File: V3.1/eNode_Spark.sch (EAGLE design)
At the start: 70 parts, among them U1 WM-N-BM-09, U10 OPA344, U2 MCP73831T-2ACI/OT, U3 R8008-33, U5 HTU21DSMD, U6 TMP006, U7 BMP180, U8 USD-SOCKETSMD, U9 MIC9.7MM, X1 USB-MICROB

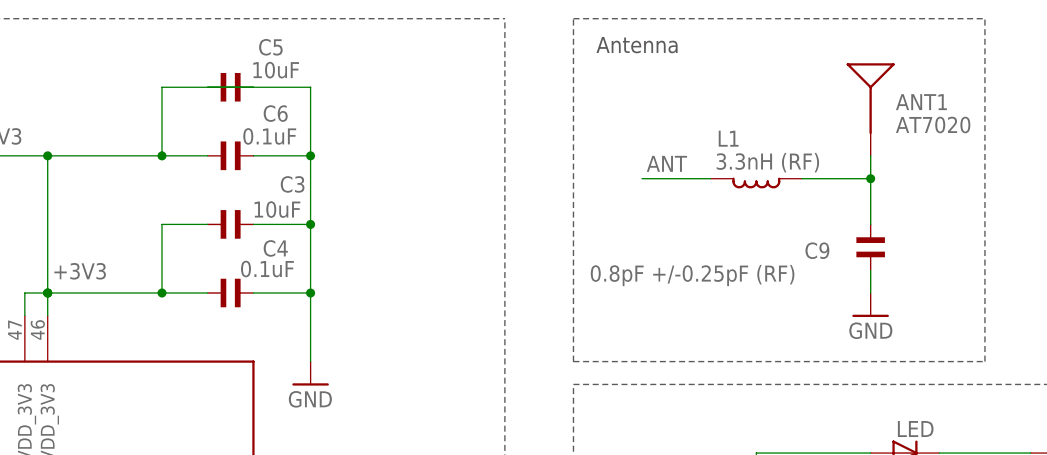
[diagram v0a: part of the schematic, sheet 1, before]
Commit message: Fully Routed
Fully Routed, DRC checked, Gerbers generated
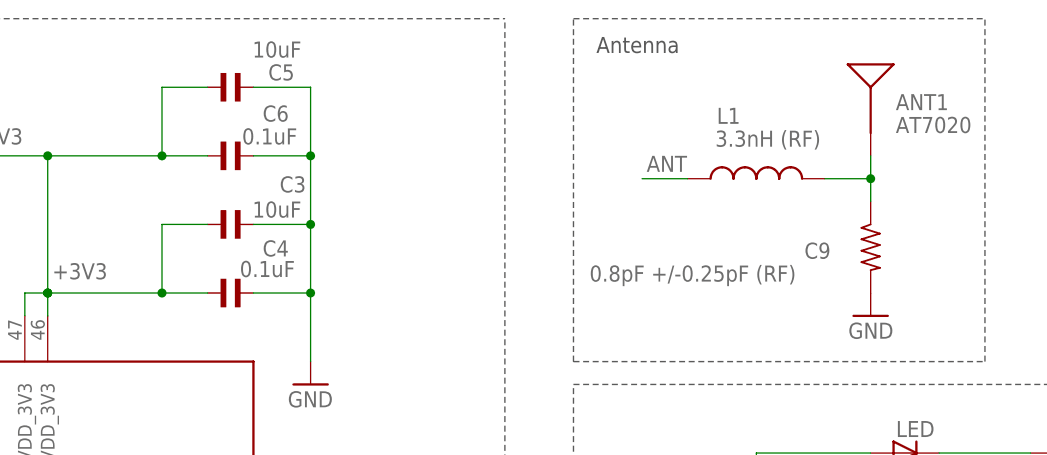
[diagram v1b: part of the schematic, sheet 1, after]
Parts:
- C9: device rc-master-smd:C_0402 -> Spark:R-US_
- L1: device rc-master-smd:L_0402 -> Spark:INDUCTOR
- R6, R7: device rc-master-smd:R_0603 -> rc-master-smd:R_0402
- renumbered LED1 to RGB_LED
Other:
- moved on the sheet: C5
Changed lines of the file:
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@@
 <setting verticaltext="up"/>
 </settings>
-<grid distance="0.1" unitdist="inch" unit="inch" style="lines" multiple="1" display="no" altdistance="0.05" altunitdist="inch" altunit="inch"/>
+<grid distance="0.1" unitdist="inch" unit="inch" style="lines" multiple="1" display="no" altdistance="0.01" altunitdist="inch" altunit="inch"/>
 <layers>
 <layer number="1" name="Top" color="4" fill="1" visible="no" active="no"/>
@@
 <part name="SUPPLY8" library="supply2" deviceset="GND" device=""/>
 <part name="+3V15" library="supply1" deviceset="+3V3" device=""/>
-<part name="R7" library="rc-master-smd" deviceset="R_" device="0603" value="4.7K"/>
-<part name="R6" library="rc-master-smd" deviceset="R_" device="0603" value="4.7K"/>
+<part name="R7" library="rc-master-smd" deviceset="R_" device="0402" value="4.7K"/>
+<part name="R6" library="rc-master-smd" deviceset="R_" device="0402" value="4.7K"/>
 <part name="GND8" library="supply1" deviceset="GND" device=""/>
 <part name="ANT1" library="Spark" deviceset="AT7020" device=""/>
-<part name="C9" library="rc-master-smd" deviceset="C_" device="0402" value="0.8pF +/-0.25pF (RF)"/>
-<part name="L1" library="rc-master-smd" deviceset="L_" device="0402" value="3.3nH (RF)"/>
+<part name="C9" library="Spark" deviceset="R-US_" device="" value="0.8pF +/-0.25pF (RF)"/>
+<part name="L1" library="Spark" deviceset="INDUCTOR" device="" value="3.3nH (RF)"/>
 <part name="R2" library="rc-master-smd" deviceset="R_" device="0402" value="100K"/>
 <part name="GND11" library="SparkFun" deviceset="GND" device=""/>
@@
 <part name="S1" library="TACT BUTTON" deviceset="TAC_SWITCH_4" device="SMD"/>
 <part name="S2" library="TACT BUTTON" deviceset="TAC_SWITCH_4" device="SMD"/>
-<part name="LED1" library="SMD RGB LED" deviceset="TOPLED-3" device="PLCC"/>
+<part name="RGB_LED" library="SMD RGB LED" deviceset="TOPLED-3" device="PLCC"/>
 <part name="U9" library="MIC" deviceset="MIC" device="9.7MM"/>
 <part name="R14" library="rc-master-smd" deviceset="R_" device="0402" value="2.2K"/>
@@
 <instance part="GND5" gate="1" x="45.72" y="134.62"/>
 <instance part="GND6" gate="1" x="120.65" y="127"/>
-<instance part="C5" gate="G$1" x="111.76" y="160.02" smashed="yes" rot="R180">
-<attribute name="NAME" x="114.808" y="163.576" size="1.778" layer="95"/>
-<attribute name="VALUE" x="114.046" y="161.036" size="1.778" layer="96"/>
+<instance part="C5" gate="G$1" x="111.76" y="160.02" smashed="yes">
+<attribute name="NAME" x="118.872" y="162.56" size="1.778" layer="95" rot="R180"/>
+<attribute name="VALUE" x="119.634" y="165.1" size="1.778" layer="96" rot="R180"/>
 </instance>
 <instance part="C1" gate="G$1" x="55.88" y="149.86" smashed="yes">
@@
 <attribute name="VALUE" x="151.638" y="140.208" size="1.778" layer="96" rot="MR180"/>
 </instance>
-<instance part="L1" gate="G$1" x="170.18" y="149.86" smashed="yes" rot="R180">
-<attribute name="NAME" x="168.402" y="155.194" size="1.778" layer="95" rot="R180"/>
-<attribute name="VALUE" x="165.608" y="150.876" size="1.778" layer="96"/>
+<instance part="L1" gate="G$1" x="170.18" y="149.86" smashed="yes" rot="R90">
+<attribute name="NAME" x="168.402" y="157.734" size="1.778" layer="95" rot="R180"/>
+<attribute name="VALUE" x="165.608" y="153.416" size="1.778" layer="96"/>
 </instance>
 <instance part="R2" gate="G$1" x="185.42" y="48.26" smashed="yes" rot="MR0">
@@
 <junction x="120.65" y="144.78"/>
 <pinref part="C5" gate="G$1" pin="2"/>
-<wire x1="109.22" y1="160.02" x2="120.65" y2="160.02" width="0.1524" layer="91"/>
+<wire x1="114.3" y1="160.02" x2="120.65" y2="160.02" width="0.1524" layer="91"/>
 <wire x1="120.65" y1="160.02" x2="120.65" y2="152.4" width="0.1524" layer="91"/>
 <junction x="120.65" y="152.4"/>
@@
 <pinref part="C9" gate="G$1" pin="2"/>
 <pinref part="GND8" gate="1" pin="GND"/>
-<wire x1="182.88" y1="137.16" x2="182.88" y2="139.7" width="0.1524" layer="91"/>
 </segment>
 <segment>
@@
 <wire x1="104.14" y1="152.4" x2="91.44" y2="152.4" width="0.1524" layer="91"/>
 <wire x1="91.44" y1="152.4" x2="78.74" y2="152.4" width="0.1524" layer="91"/>
-<wire x1="114.3" y1="160.02" x2="104.14" y2="160.02" width="0.1524" layer="91"/>
+<wire x1="109.22" y1="160.02" x2="104.14" y2="160.02" width="0.1524" layer="91"/>
 <wire x1="71.12" y1="152.4" x2="78.74" y2="152.4" width="0.1524" layer="91"/>
 <pinref part="U1" gate="G$1" pin="VDD_3V3@47"/>
@@
 </segment>
 <segment>
-<wire x1="157.48" y1="149.86" x2="165.1" y2="149.86" width="0.1524" layer="91"/>
+<wire x1="157.48" y1="149.86" x2="162.56" y2="149.86" width="0.1524" layer="91"/>
 <pinref part="L1" gate="G$1" pin="1"/>
 <label x="157.988" y="150.622" size="1.778" layer="95"/>
@@
 <net name="N$1" class="2">
 <segment>
-<wire x1="175.26" y1="149.86" x2="182.88" y2="149.86" width="0.1524" layer="91"/>
+<wire x1="177.8" y1="149.86" x2="182.88" y2="149.86" width="0.1524" layer="91"/>
 <wire x1="182.88" y1="149.86" x2="182.88" y2="152.4" width="0.1524" layer="91"/>
-<wire x1="182.88" y1="144.78" x2="182.88" y2="149.86" width="0.1524" layer="91"/>
+<wire x1="182.88" y1="147.32" x2="182.88" y2="149.86" width="0.1524" layer="91"/>
 <junction x="182.88" y="149.86"/>
 <pinref part="ANT1" gate="G$1" pin="SIGNAL"/>
@@
 <instance part="S1" gate="S" x="40.64" y="73.66" rot="R90"/>
 <instance part="S2" gate="S" x="58.42" y="73.66" rot="R90"/>
-<instance part="LED1" gate="G$1" x="43.18" y="24.13" rot="MR270"/>
+<instance part="RGB_LED" gate="G$1" x="43.18" y="24.13" rot="MR270"/>
 <instance part="U9" gate="G$1" x="157.48" y="66.04" rot="R90"/>
 <instance part="R14" gate="G$1" x="162.56" y="76.2" rot="R270"/>
@@
 <wire x1="35.56" y1="35.56" x2="35.56" y2="29.21" width="0.1524" layer="91"/>
 <wire x1="35.56" y1="29.21" x2="38.1" y2="29.21" width="0.1524" layer="91"/>
-<pinref part="LED1" gate="G$1" pin="A2"/>
+<pinref part="RGB_LED" gate="G$1" pin="A2"/>
 </segment>
 <segment>
@@
 <wire x1="45.72" y1="24.13" x2="55.88" y2="24.13" width="0.1524" layer="91"/>
 <pinref part="R10" gate="G$1" pin="1"/>
-<pinref part="LED1" gate="G$1" pin="CGREEN"/>
+<pinref part="RGB_LED" gate="G$1" pin="CGREEN"/>
 </segment>
 </net>
@@
 <wire x1="45.72" y1="19.05" x2="55.88" y2="19.05" width="0.1524" layer="91"/>
 <pinref part="R11" gate="G$1" pin="1"/>
-<pinref part="LED1" gate="G$1" pin="CBLUE"/>
+<pinref part="RGB_LED" gate="G$1" pin="CBLUE"/>
 </segment>
 </net>
@@
 <wire x1="45.72" y1="29.21" x2="55.88" y2="29.21" width="0.1524" layer="91"/>
 <pinref part="R9" gate="G$1" pin="1"/>
-<pinref part="LED1" gate="G$1" pin="CRED"/>
-</segment>
-</net>
+<pinref part="RGB_LED" gate="G$1" pin="CRED"/>
+</segment>
+</net>
